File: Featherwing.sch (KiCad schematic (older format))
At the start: 15 parts, among them J2 CONN_01X16, J3 CONN_01X12, J5 GROVE-CONNECTOR-SMD-90D(4+2P-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, U2 ROF-78E

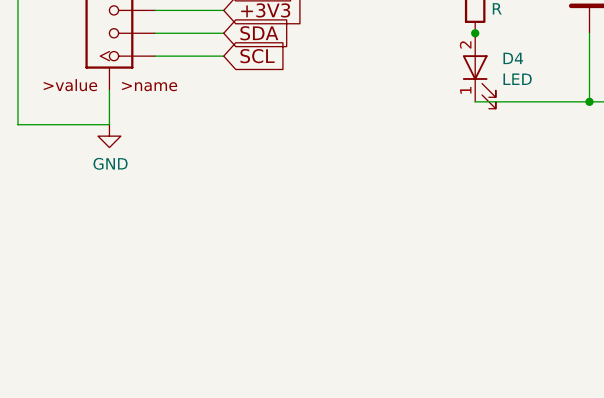
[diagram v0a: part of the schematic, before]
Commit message: Added more parts to featherwing
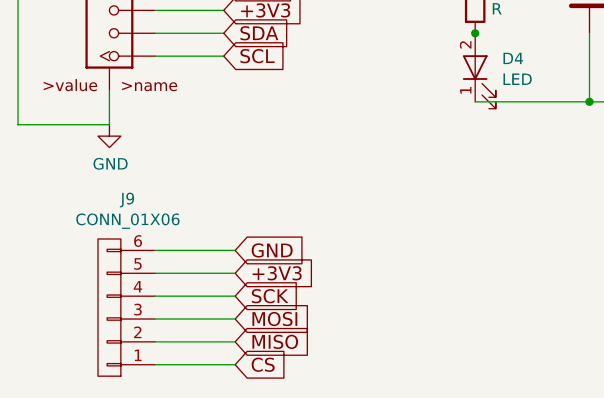
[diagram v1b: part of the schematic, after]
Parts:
- added J9: CONN_01X06, symbol CONN_01X06
- JP1: footprint (none) -> Wire_Connections_Bridges:WireConnection_0.80mmDrill
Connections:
- net +3V3: now also J9.5 (P5)
- net CS: now also J9.1 (P1)
- net GND: now also J9.6 (P6)
- net MISO: now also J9.2 (P2)
- net MOSI: now also J9.3 (P3)
- net SCK: now also J9.4 (P4)
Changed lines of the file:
@@
 F 0 "JP1" H 5400 3112 50  0000 C CNN
 F 1 "Jumper_NC_Small" H 5400 3021 50  0000 C CNN
-F 2 "" H 300 -450 50  0001 C CNN
+F 2 "Wire_Connections_Bridges:WireConnection_0.80mmDrill" H 300 -450 50  0001 C CNN
 F 3 "" H 300 -450 50  0001 C CNN
 	1    5400 2900
@@
 UC
 $Comp
-L GND #PWR014
+L GND #PWR15
 U 1 1 58E27B40
 P 6800 3500
-F 0 "#PWR014" H 6850 3550 50  0001 C CNN
+F 0 "#PWR15" H 6850 3550 50  0001 C CNN
 F 1 "GND" H 6805 3327 50  0000 C CNN
 F 2 "" H 100 -150 50  0001 C CNN
@@
 $EndComp
 $Comp
-L GND #PWR015
+L GND #PWR14
 U 1 1 58E27FEA
 P 3600 3600
-F 0 "#PWR015" H 3650 3650 50  0001 C CNN
+F 0 "#PWR14" H 3650 3650 50  0001 C CNN
 F 1 "GND" H 3605 3427 50  0000 C CNN
 F 2 "" H -3100 -50 50  0001 C CNN
@@
 Text GLabel 4600 900  1    60   Input ~ 0
 CS
+$Comp
+L CONN_01X06 J9
+U 1 1 58F503C4
+P 3600 4400
+F 0 "J9" H 3519 3925 50  0000 C CNN
+F 1 "CONN_01X06" H 3519 4016 50  0000 C CNN
+F 2 "" H 0   -150 50  0001 C CNN
+F 3 "" H 0   -150 50  0001 C CNN
+	1    3600 4400
+	-1   0    0    1
+$EndComp
+Wire Wire Line
+	3800 4150 4150 4150
+Wire Wire Line
+	3800 4250 4150 4250
+Wire Wire Line
+	3800 4350 4150 4350
+Wire Wire Line
+	3800 4450 4150 4450
+Wire Wire Line
+	3800 4550 4150 4550
+Wire Wire Line
+	3800 4650 4150 4650
+Text GLabel 4150 4150 2    60   Input ~ 0
+GND
+Text GLabel 4150 4250 2    60   Input ~ 0
++3V3
+Text GLabel 4150 4350 2    60   Input ~ 0
+SCK
+Text GLabel 4150 4450 2    60   Input ~ 0
+MOSI
+Text GLabel 4150 4550 2    60   Input ~ 0
+MISO
+Text GLabel 4150 4650 2    60   Input ~ 0
+CS
 $EndSCHEMATC

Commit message: Laid out most parts within PCB bounds
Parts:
- J9: footprint (none) -> Connectors_JST:JST_PH_B6B-PH-SM4-TB_06x2.00mm_Straight
- JP1: footprint Wire_Connections_Bridges:WireConnection_0.80mmDrill -> Connect:GS2
- R1: footprint Resistors_SMD:R_0603 -> Resistors_SMD:R_0603_HandSoldering
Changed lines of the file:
@@
 F 0 "R1" H 5270 3096 50  0000 L CNN
 F 1 "R" H 5270 3005 50  0000 L CNN
-F 2 "Resistors_SMD:R_0603" V -70 150 50  0001 C CNN
+F 2 "Resistors_SMD:R_0603_HandSoldering" V -70 150 50  0001 C CNN
 F 3 "" H 0   150 50  0001 C CNN
 	1    5200 3050
@@
 F 0 "JP1" H 5400 3112 50  0000 C CNN
 F 1 "Jumper_NC_Small" H 5400 3021 50  0000 C CNN
-F 2 "Wire_Connections_Bridges:WireConnection_0.80mmDrill" H 300 -450 50  0001 C CNN
+F 2 "Connect:GS2" H 300 -450 50  0001 C CNN
 F 3 "" H 300 -450 50  0001 C CNN
 	1    5400 2900
@@
 UC
 $Comp
-L GND #PWR15
+L GND #PWR018
 U 1 1 58E27B40
 P 6800 3500
-F 0 "#PWR15" H 6850 3550 50  0001 C CNN
+F 0 "#PWR018" H 6850 3550 50  0001 C CNN
 F 1 "GND" H 6805 3327 50  0000 C CNN
 F 2 "" H 100 -150 50  0001 C CNN
@@
 $EndComp
 $Comp
-L GND #PWR14
+L GND #PWR019
 U 1 1 58E27FEA
 P 3600 3600
-F 0 "#PWR14" H 3650 3650 50  0001 C CNN
+F 0 "#PWR019" H 3650 3650 50  0001 C CNN
 F 1 "GND" H 3605 3427 50  0000 C CNN
 F 2 "" H -3100 -50 50  0001 C CNN
@@
 F 0 "J9" H 3519 3925 50  0000 C CNN
 F 1 "CONN_01X06" H 3519 4016 50  0000 C CNN
-F 2 "" H 0   -150 50  0001 C CNN
+F 2 "Connectors_JST:JST_PH_B6B-PH-SM4-TB_06x2.00mm_Straight" H 0   -150 50  0001 C CNN
 F 3 "" H 0   -150 50  0001 C CNN
 	1    3600 4400

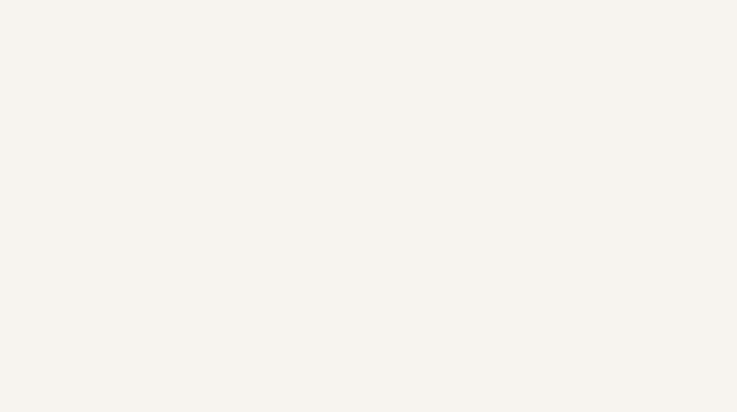
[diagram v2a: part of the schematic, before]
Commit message: Added JST footprints, mounting holes and logos
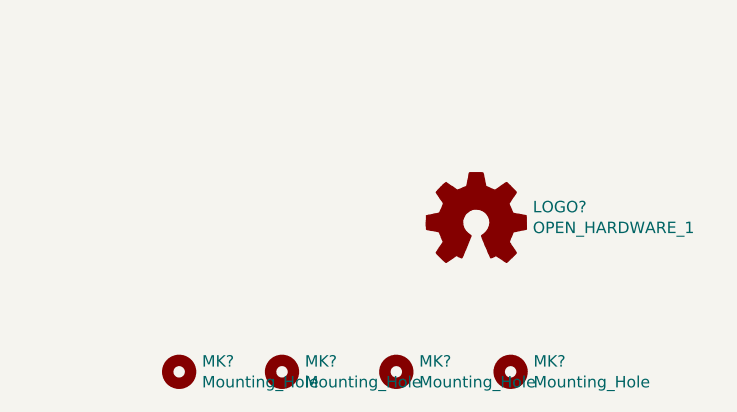
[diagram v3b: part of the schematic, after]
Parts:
- added LOGO?: OPEN_HARDWARE_1, symbol OPEN_HARDWARE_1
- added MK? (x4): Mounting_Hole, symbol Mounting_Hole
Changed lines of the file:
@@
 LIBS:ROF-78E
 LIBS:GROVE-CONNECTOR-SMD
+LIBS:logo
+LIBS:mechanical
 LIBS:V9203_Devkit-cache
 EELAYER 26 0
@@
 UC
 $Comp
-L GND #PWR018
+L GND #PWR019
 U 1 1 58E27B40
 P 6800 3500
-F 0 "#PWR018" H 6850 3550 50  0001 C CNN
+F 0 "#PWR019" H 6850 3550 50  0001 C CNN
 F 1 "GND" H 6805 3327 50  0000 C CNN
 F 2 "" H 100 -150 50  0001 C CNN
@@
 $EndComp
 $Comp
-L GND #PWR019
+L GND #PWR020
 U 1 1 58E27FEA
 P 3600 3600
-F 0 "#PWR019" H 3650 3650 50  0001 C CNN
+F 0 "#PWR020" H 3650 3650 50  0001 C CNN
 F 1 "GND" H 3605 3427 50  0000 C CNN
 F 2 "" H -3100 -50 50  0001 C CNN
@@
 Text GLabel 4150 4650 2    60   Input ~ 0
 CS
+$Comp
+L OPEN_HARDWARE_1 LOGO?
+U 1 1 58FEBF9A
+P 8350 4700
+F 0 "LOGO?" H 8597 4771 50  0000 L CNN
+F 1 "OPEN_HARDWARE_1" H 8597 4680 50  0000 L CNN
+F 2 "" H 1450 -250 50  0001 C CNN
+F 3 "" H 1450 -250 50  0001 C CNN
+	1    8350 4700
+	1    0    0    -1
+$EndComp
+$Comp
+L Mounting_Hole MK?
+U 1 1 58FEC0CD
+P 7050 5350
+F 0 "MK?" H 7150 5396 50  0000 L CNN
+F 1 "Mounting_Hole" H 7150 5305 50  0000 L CNN
+F 2 "" H -1150 -50 50  0001 C CNN
+F 3 "" H -1150 -50 50  0001 C CNN
+	1    7050 5350
+	1    0    0    -1
+$EndComp
+$Comp
+L Mounting_Hole MK?
+U 1 1 58FEC187
+P 7500 5350
+F 0 "MK?" H 7600 5396 50  0000 L CNN
+F 1 "Mounting_Hole" H 7600 5305 50  0000 L CNN
+F 2 "" H -700 -50 50  0001 C CNN
+F 3 "" H -700 -50 50  0001 C CNN
+	1    7500 5350
+	1    0    0    -1
+$EndComp
+$Comp
+L Mounting_Hole MK?
+U 1 1 58FEC1E1
+P 8000 5350
+F 0 "MK?" H 8100 5396 50  0000 L CNN
+F 1 "Mounting_Hole" H 8100 5305 50  0000 L CNN
+F 2 "" H -200 -50 50  0001 C CNN
+F 3 "" H -200 -50 50  0001 C CNN
+	1    8000 5350
+	1    0    0    -1
+$EndComp
+$Comp
+L Mounting_Hole MK?
+U 1 1 58FEC23B
+P 8500 5350
+F 0 "MK?" H 8600 5396 50  0000 L CNN
+F 1 "Mounting_Hole" H 8600 5305 50  0000 L CNN
+F 2 "" H 300 -50 50  0001 C CNN
+F 3 "" H 300 -50 50  0001 C CNN
+	1    8500 5350
+	1    0    0    -1
+$EndComp
 $EndSCHEMATC
